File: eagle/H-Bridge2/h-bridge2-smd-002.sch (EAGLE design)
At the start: 38 parts

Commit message: SMD for logic drv
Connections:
- net N$1: now also U$1.IP+; no longer U$1.IP-
- net N$17: now also U$1.IP-; no longer U$1.IP+
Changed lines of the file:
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@@
 <wire x1="-50.8" y1="7.62" x2="-50.8" y2="10.16" width="0.1524" layer="91"/>
 <wire x1="-50.8" y1="10.16" x2="-63.5" y2="10.16" width="0.1524" layer="91"/>
-<wire x1="-63.5" y1="10.16" x2="-63.5" y2="-10.16" width="0.1524" layer="91"/>
-<pinref part="U$1" gate="G$1" pin="IP+"/>
-<wire x1="-63.5" y1="-10.16" x2="-45.72" y2="-10.16" width="0.1524" layer="91"/>
+<wire x1="-63.5" y1="10.16" x2="-63.5" y2="-12.7" width="0.1524" layer="91"/>
 <junction x="-15.24" y="99.06"/>
+<wire x1="-63.5" y1="-12.7" x2="-50.8" y2="-12.7" width="0.1524" layer="91"/>
+<wire x1="-50.8" y1="-12.7" x2="-50.8" y2="-20.32" width="0.1524" layer="91"/>
+<pinref part="U$1" gate="G$1" pin="IP-"/>
+<wire x1="-50.8" y1="-20.32" x2="-45.72" y2="-20.32" width="0.1524" layer="91"/>
 </segment>
 </net>
@@
 <net name="N$1" class="0">
 <segment>
-<pinref part="U$1" gate="G$1" pin="IP-"/>
-<wire x1="-45.72" y1="-20.32" x2="-66.04" y2="-20.32" width="0.1524" layer="91"/>
 <wire x1="-66.04" y1="-20.32" x2="-66.04" y2="-30.48" width="0.1524" layer="91"/>
 <pinref part="JP_MA2" gate="G$1" pin="1"/>
 <wire x1="-66.04" y1="-30.48" x2="-53.34" y2="-30.48" width="0.1524" layer="91"/>
-</segment>
-</net>
+<wire x1="-66.04" y1="-20.32" x2="-55.88" y2="-20.32" width="0.1524" layer="91"/>
+<wire x1="-55.88" y1="-20.32" x2="-55.88" y2="-10.16" width="0.1524" layer="91"/>
+<pinref part="U$1" gate="G$1" pin="IP+"/>
+<wire x1="-55.88" y1="-10.16" x2="-45.72" y2="-10.16" width="0.1524" layer="91"/>
+</segment>
+</net>

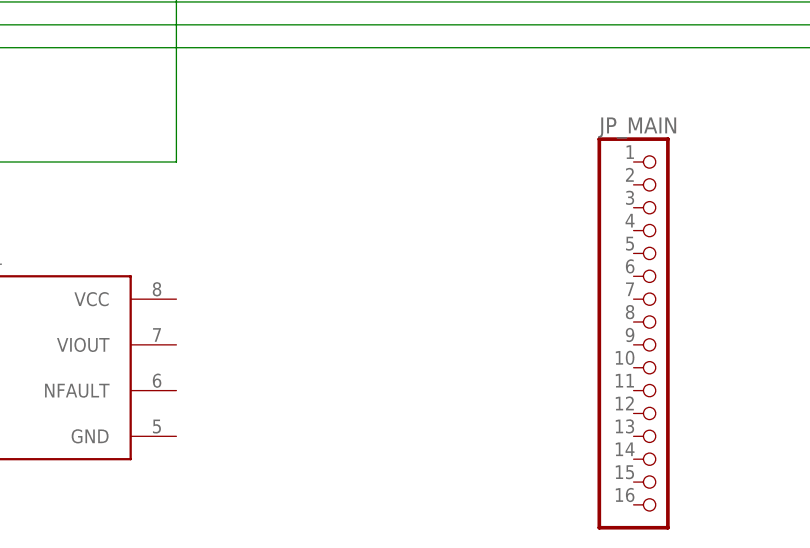
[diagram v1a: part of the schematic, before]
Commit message: SMD for logic drv
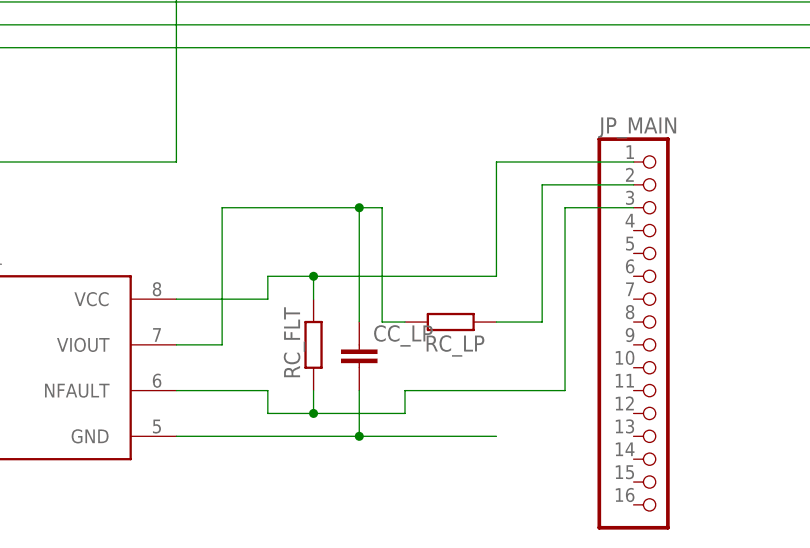
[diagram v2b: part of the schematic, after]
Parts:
- added CC_LP: (no value), rcl:C-EUC4532
- added RC_FLT, RC_LP: (no value), rcl:R-EU_R1206
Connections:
- new net N$15: CC_LP.1, RC_LP.2, U$1.VIOUT
- new net N$19: JP_MAIN.2, RC_LP.1
- new net N$2: JP_MAIN.1, RC_FLT.2, U$1.VCC
- new net N$21: CC_LP.2, U$1.GND
- new net N$3: JP_MAIN.3, RC_FLT.1, U$1.NFAULT
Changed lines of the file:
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@@
 <part name="U$1" library="acs711" deviceset="ACS711" device=""/>
 <part name="JP_MA2" library="dbg-misc" deviceset="PINHD-1X1" device=""/>
+<part name="RC_LP" library="rcl" deviceset="R-EU_" device="R1206"/>
+<part name="RC_FLT" library="rcl" deviceset="R-EU_" device="R1206"/>
+<part name="CC_LP" library="rcl" deviceset="C-EU" device="C4532"/>
 </parts>
 <sheets>
@@
 <instance part="U$1" gate="G$1" x="-30.48" y="-15.24"/>
 <instance part="JP_MA2" gate="G$1" x="-50.8" y="-30.48"/>
+<instance part="RC_LP" gate="G$1" x="15.24" y="-10.16" rot="R180"/>
+<instance part="RC_FLT" gate="G$1" x="0" y="-12.7" rot="R90"/>
+<instance part="CC_LP" gate="G$1" x="5.08" y="-12.7"/>
 </instances>
 <busses>
@@
 </segment>
 </net>
+<net name="N$2" class="0">
+<segment>
+<pinref part="U$1" gate="G$1" pin="VCC"/>
+<wire x1="-15.24" y1="-7.62" x2="-5.08" y2="-7.62" width="0.1524" layer="91"/>
+<wire x1="-5.08" y1="-7.62" x2="-5.08" y2="-5.08" width="0.1524" layer="91"/>
+<wire x1="-5.08" y1="-5.08" x2="0" y2="-5.08" width="0.1524" layer="91"/>
+<junction x="0" y="-5.08"/>
+<pinref part="RC_FLT" gate="G$1" pin="2"/>
+<wire x1="0" y1="-5.08" x2="0" y2="-7.62" width="0.1524" layer="91"/>
+<wire x1="0" y1="-5.08" x2="20.32" y2="-5.08" width="0.1524" layer="91"/>
+<wire x1="20.32" y1="-5.08" x2="20.32" y2="7.62" width="0.1524" layer="91"/>
+<pinref part="JP_MAIN" gate="A" pin="1"/>
+<wire x1="20.32" y1="7.62" x2="35.56" y2="7.62" width="0.1524" layer="91"/>
+</segment>
+</net>
+<net name="N$3" class="0">
+<segment>
+<pinref part="U$1" gate="G$1" pin="NFAULT"/>
+<wire x1="-15.24" y1="-17.78" x2="-5.08" y2="-17.78" width="0.1524" layer="91"/>
+<wire x1="-5.08" y1="-17.78" x2="-5.08" y2="-20.32" width="0.1524" layer="91"/>
+<wire x1="-5.08" y1="-20.32" x2="0" y2="-20.32" width="0.1524" layer="91"/>
+<pinref part="RC_FLT" gate="G$1" pin="1"/>
+<wire x1="0" y1="-17.78" x2="0" y2="-20.32" width="0.1524" layer="91"/>
+<junction x="0" y="-20.32"/>
+<wire x1="0" y1="-20.32" x2="10.16" y2="-20.32" width="0.1524" layer="91"/>
+<wire x1="10.16" y1="-20.32" x2="10.16" y2="-17.78" width="0.1524" layer="91"/>
+<wire x1="10.16" y1="-17.78" x2="27.94" y2="-17.78" width="0.1524" layer="91"/>
+<wire x1="27.94" y1="-17.78" x2="27.94" y2="2.54" width="0.1524" layer="91"/>
+<pinref part="JP_MAIN" gate="A" pin="3"/>
+<wire x1="27.94" y1="2.54" x2="35.56" y2="2.54" width="0.1524" layer="91"/>
+</segment>
+</net>
+<net name="N$15" class="0">
+<segment>
+<pinref part="U$1" gate="G$1" pin="VIOUT"/>
+<wire x1="-15.24" y1="-12.7" x2="-10.16" y2="-12.7" width="0.1524" layer="91"/>
+<wire x1="-10.16" y1="-12.7" x2="-10.16" y2="2.54" width="0.1524" layer="91"/>
+<wire x1="-10.16" y1="2.54" x2="5.08" y2="2.54" width="0.1524" layer="91"/>
+<wire x1="5.08" y1="2.54" x2="7.62" y2="2.54" width="0.1524" layer="91"/>
+<wire x1="7.62" y1="2.54" x2="7.62" y2="-10.16" width="0.1524" layer="91"/>
+<pinref part="RC_LP" gate="G$1" pin="2"/>
+<wire x1="7.62" y1="-10.16" x2="10.16" y2="-10.16" width="0.1524" layer="91"/>
+<pinref part="CC_LP" gate="G$1" pin="1"/>
+<wire x1="5.08" y1="-10.16" x2="5.08" y2="2.54" width="0.1524" layer="91"/>
+<junction x="5.08" y="2.54"/>
+</segment>
+</net>
+<net name="N$19" class="0">
+<segment>
+<pinref part="RC_LP" gate="G$1" pin="1"/>
+<wire x1="20.32" y1="-10.16" x2="25.4" y2="-10.16" width="0.1524" layer="91"/>
+<wire x1="25.4" y1="-10.16" x2="25.4" y2="5.08" width="0.1524" layer="91"/>
+<pinref part="JP_MAIN" gate="A" pin="2"/>
+<wire x1="25.4" y1="5.08" x2="35.56" y2="5.08" width="0.1524" layer="91"/>
+</segment>
+</net>
+<net name="N$21" class="0">
+<segment>
+<pinref part="U$1" gate="G$1" pin="GND"/>
+<wire x1="-15.24" y1="-22.86" x2="5.08" y2="-22.86" width="0.1524" layer="91"/>
+<pinref part="CC_LP" gate="G$1" pin="2"/>
+<wire x1="5.08" y1="-22.86" x2="20.32" y2="-22.86" width="0.1524" layer="91"/>
+<wire x1="5.08" y1="-17.78" x2="5.08" y2="-22.86" width="0.1524" layer="91"/>
+<junction x="5.08" y="-22.86"/>
+</segment>
+</net>

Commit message: Drv signals wiring
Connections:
- removed net N$27: JP1.6, UB.SD
- net N$20: now also UB.SD
- net N$21: now also JP_MAIN.4
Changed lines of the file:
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@@
 <pinref part="UA" gate="A" pin="SD"/>
 <wire x1="-106.68" y1="83.82" x2="-137.16" y2="83.82" width="0.1524" layer="91"/>
-<wire x1="-137.16" y1="83.82" x2="-137.16" y2="22.86" width="0.1524" layer="91"/>
+<wire x1="-137.16" y1="83.82" x2="-137.16" y2="35.56" width="0.1524" layer="91"/>
+<wire x1="-137.16" y1="35.56" x2="-137.16" y2="22.86" width="0.1524" layer="91"/>
 <wire x1="-137.16" y1="22.86" x2="-91.44" y2="22.86" width="0.1524" layer="91"/>
 <wire x1="-91.44" y1="22.86" x2="-91.44" y2="25.4" width="0.1524" layer="91"/>
 <pinref part="JP1" gate="A" pin="3"/>
 <wire x1="-91.44" y1="25.4" x2="-83.82" y2="25.4" width="0.1524" layer="91"/>
+<pinref part="UB" gate="A" pin="SD"/>
+<wire x1="114.3" y1="83.82" x2="119.38" y2="83.82" width="0.1524" layer="91"/>
+<wire x1="119.38" y1="83.82" x2="119.38" y2="101.6" width="0.1524" layer="91"/>
+<wire x1="119.38" y1="101.6" x2="175.26" y2="101.6" width="0.1524" layer="91"/>
+<wire x1="175.26" y1="101.6" x2="175.26" y2="22.86" width="0.1524" layer="91"/>
+<wire x1="175.26" y1="22.86" x2="-60.96" y2="22.86" width="0.1524" layer="91"/>
+<wire x1="-137.16" y1="35.56" x2="-60.96" y2="35.56" width="0.1524" layer="91"/>
+<wire x1="-60.96" y1="35.56" x2="-60.96" y2="22.86" width="0.1524" layer="91"/>
+<junction x="-137.16" y="35.56"/>
 </segment>
 </net>
@@
 </segment>
 </net>
-<net name="N$27" class="0">
-<segment>
-<pinref part="UB" gate="A" pin="SD"/>
-<wire x1="114.3" y1="83.82" x2="119.38" y2="83.82" width="0.1524" layer="91"/>
-<wire x1="119.38" y1="83.82" x2="119.38" y2="101.6" width="0.1524" layer="91"/>
-<wire x1="119.38" y1="101.6" x2="175.26" y2="101.6" width="0.1524" layer="91"/>
-<wire x1="175.26" y1="101.6" x2="175.26" y2="22.86" width="0.1524" layer="91"/>
-<wire x1="175.26" y1="22.86" x2="-76.2" y2="22.86" width="0.1524" layer="91"/>
-<pinref part="JP1" gate="A" pin="6"/>
-</segment>
-</net>
 <net name="N$28" class="0">
 <segment>
@@
 <wire x1="-15.24" y1="-22.86" x2="5.08" y2="-22.86" width="0.1524" layer="91"/>
 <pinref part="CC_LP" gate="G$1" pin="2"/>
-<wire x1="5.08" y1="-22.86" x2="20.32" y2="-22.86" width="0.1524" layer="91"/>
+<wire x1="5.08" y1="-22.86" x2="22.86" y2="-22.86" width="0.1524" layer="91"/>
 <wire x1="5.08" y1="-17.78" x2="5.08" y2="-22.86" width="0.1524" layer="91"/>
 <junction x="5.08" y="-22.86"/>
-</segment>
-</net>
+<wire x1="22.86" y1="-22.86" x2="22.86" y2="0" width="0.1524" layer="91"/>
+<pinref part="JP_MAIN" gate="A" pin="4"/>
+<wire x1="22.86" y1="0" x2="35.56" y2="0" width="0.1524" layer="91"/>
+</segment>
+</net>

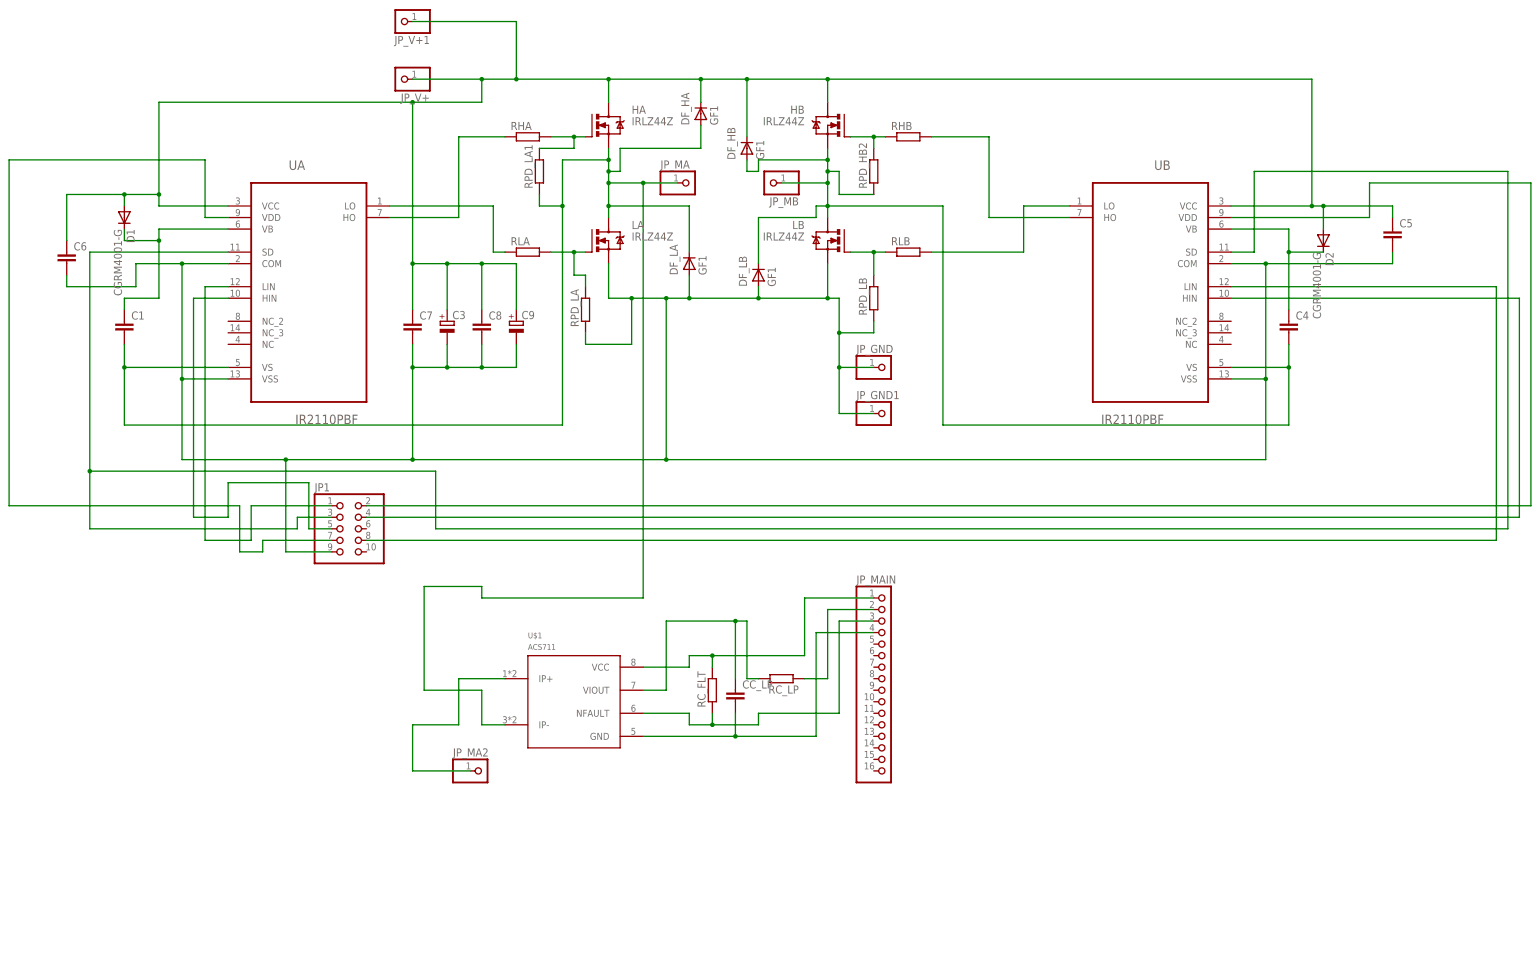
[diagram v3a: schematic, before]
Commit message: Hbr wiring 0 airways, no polygon
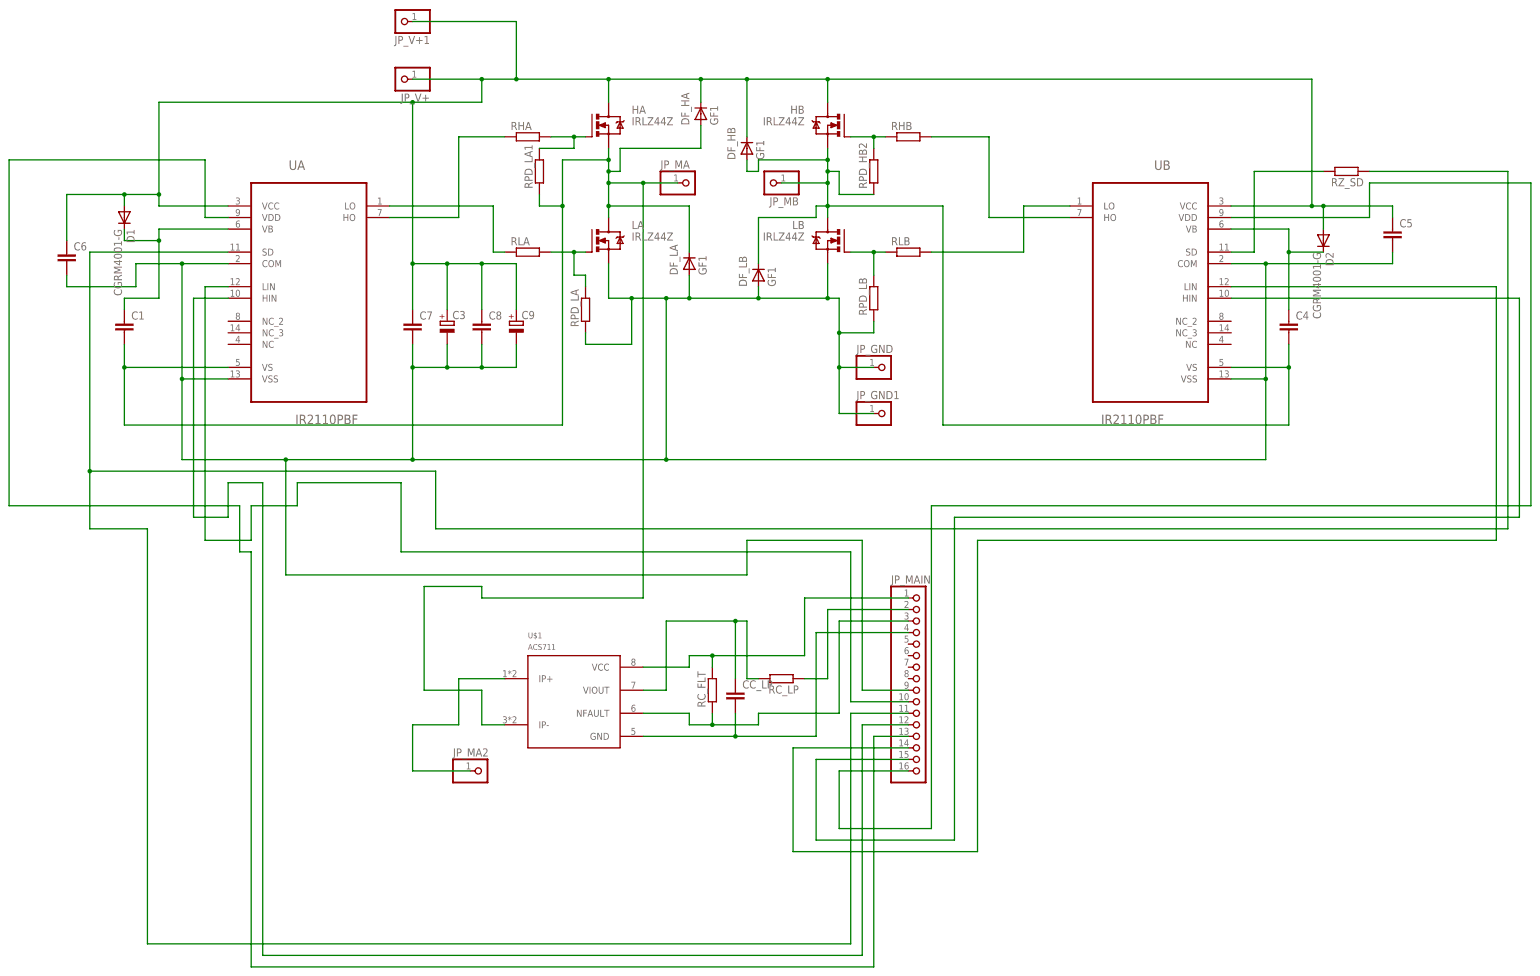
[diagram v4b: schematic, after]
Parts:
- removed JP1: (no value), pinhead:PINHD-2X5
- added RZ_SD: (no value), rcl:R-EU_R1206
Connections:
- new net N$27: JP_MAIN.14, UB.LIN
- net N$20: now also JP_MAIN.11, RZ_SD.1; no longer JP1.3, UB.SD
- net N$22: now also JP_MAIN.13; no longer JP1.7
- net N$23: now also JP_MAIN.12; no longer JP1.5
- net N$24: now also JP_MAIN.10; no longer JP1.1
- net N$25: now also JP_MAIN.16; no longer JP1.2
- net N$26: now also JP_MAIN.15; no longer JP1.4
- net N$28: now also RZ_SD.2, UB.SD; no longer JP1.8, UB.LIN
- net N$4: now also JP_MAIN.9; no longer JP1.9
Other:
- moved on the sheet: JP_MAIN
